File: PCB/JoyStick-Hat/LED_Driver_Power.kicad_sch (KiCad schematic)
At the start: 1 part, among them U2 STP16CPC26XTR

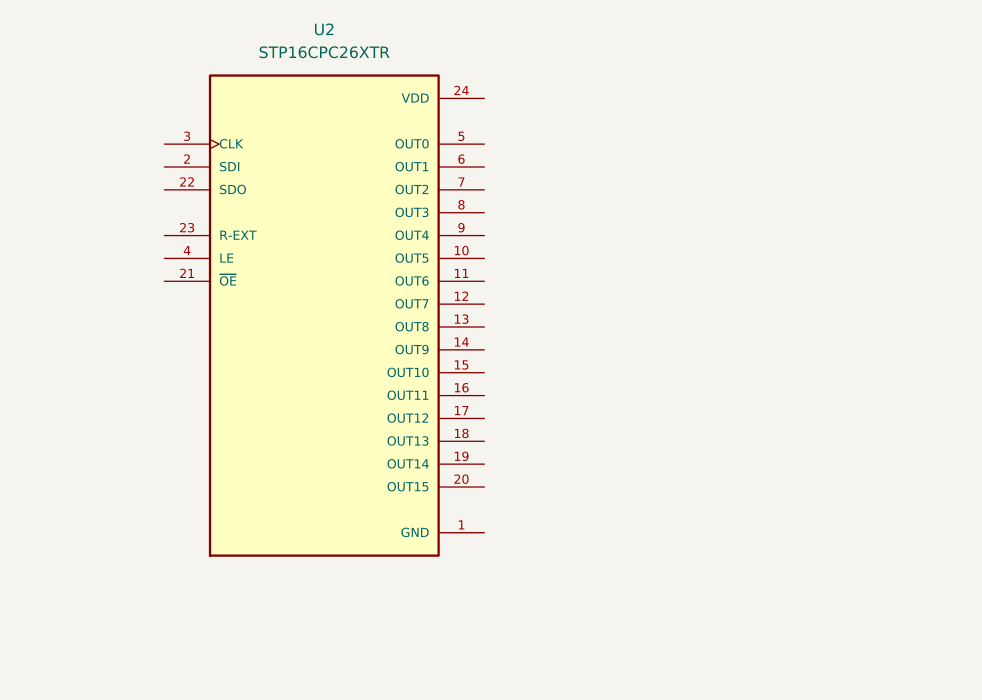
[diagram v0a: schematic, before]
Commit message: Power and LED Driver
Power Supply Schematic sketched out using Pololu power regulator modules to hasten design. LED drivers replaced with ones that have 24 ouputs so we can use 20 unit bar graph LEDs and have 8 extra channels for other onboard LEDs
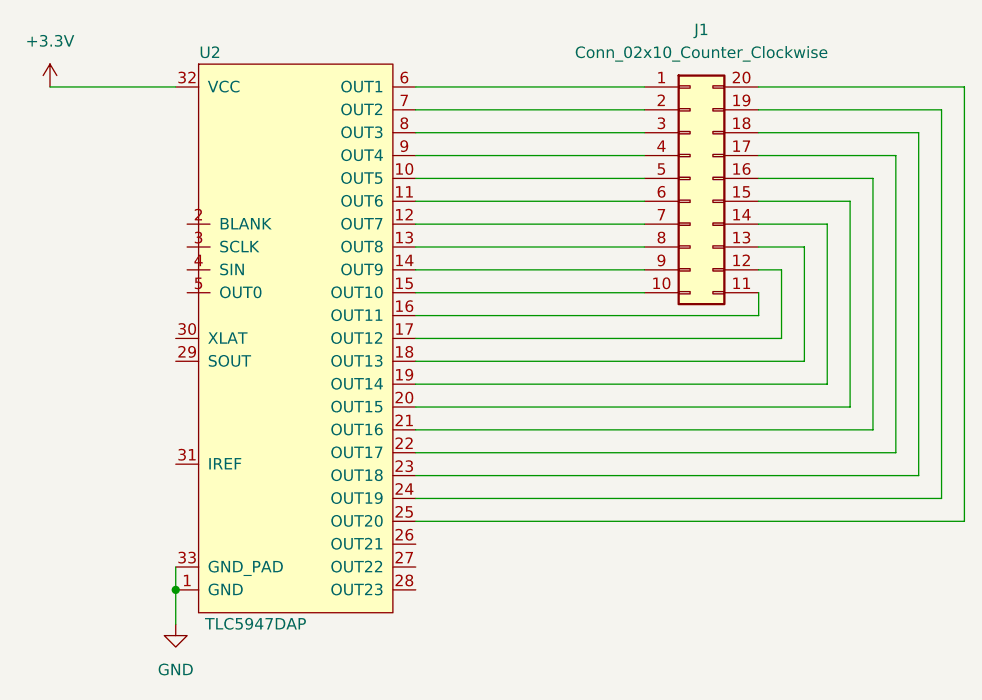
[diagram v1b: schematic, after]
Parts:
- removed U2: STP16CPC26XTR, AVR-KiCAD-Lib-ICs:SOP63P600X173-24N_STP16CPC26XTR, symbol AVR-KiCAD-Lib-ICs:STP16CPC26XTR
- added J1: Conn_02x10_Counter_Clockwise, Connector_PinHeader_2.54mm:PinHeader_2x10_P2.54mm_Vertical, symbol Connector_Generic:Conn_02x10_Counter_Clockwise
- added U2: TLC5947DAP, AVR-KiCAD-Lib-ICs:DAP32_4P36X4P11, symbol AVR-KiCAD-Lib-ICs:TLC5947DAP
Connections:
- new net: J1.1 (Pin_1), U2.6 (OUT1)
- new net: J1.10 (Pin_10), U2.15 (OUT10)
- new net: J1.11 (Pin_11), U2.16 (OUT11)
- new net: J1.12 (Pin_12), U2.17 (OUT12)
- new net: J1.13 (Pin_13), U2.18 (OUT13)
- new net: J1.14 (Pin_14), U2.19 (OUT14)
- new net: J1.15 (Pin_15), U2.20 (OUT15)
- new net: J1.16 (Pin_16), U2.21 (OUT16)
- new net: J1.17 (Pin_17), U2.22 (OUT17)
- new net: J1.18 (Pin_18), U2.23 (OUT18)
- new net: J1.19 (Pin_19), U2.24 (OUT19)
- new net: J1.2 (Pin_2), U2.7 (OUT2)
- new net: J1.20 (Pin_20), U2.25 (OUT20)
- new net: J1.3 (Pin_3), U2.8 (OUT3)
- new net: J1.4 (Pin_4), U2.9 (OUT4)
- new net: J1.5 (Pin_5), U2.10 (OUT5)
- new net: J1.6 (Pin_6), U2.11 (OUT6)
- new net: J1.7 (Pin_7), U2.12 (OUT7)
- new net: J1.8 (Pin_8), U2.13 (OUT8)
- new net: J1.9 (Pin_9), U2.14 (OUT9)
- new net +3.3V: U2.32 (VCC)
- new net GND: U2.1 (GND), U2.33 (GND_PAD)

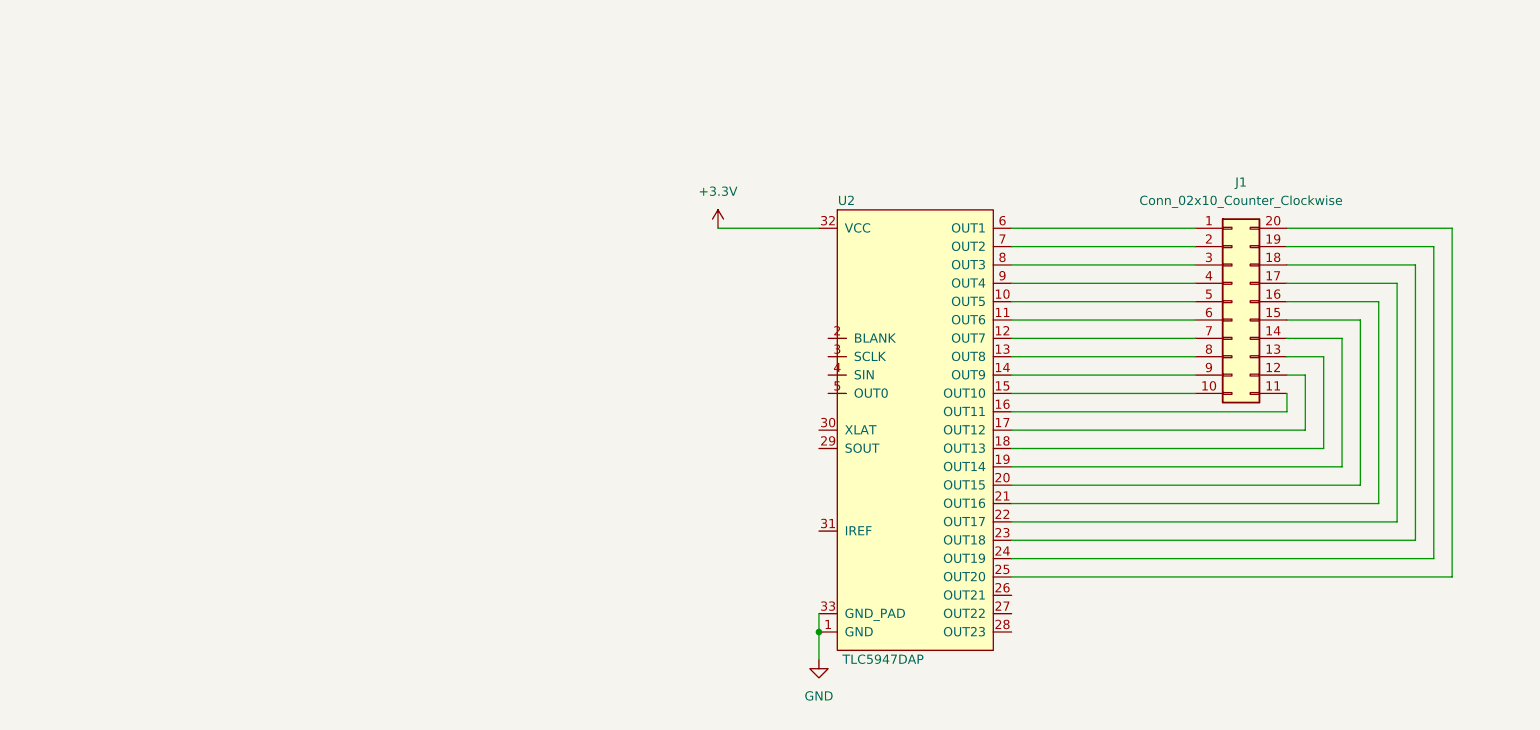
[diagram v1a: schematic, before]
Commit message: LED drivers and Joystick
Finished LED driver scheamtics, corrected some problems with symbols. added conenctors for joystick and buttons, connected RPI pins to MCU
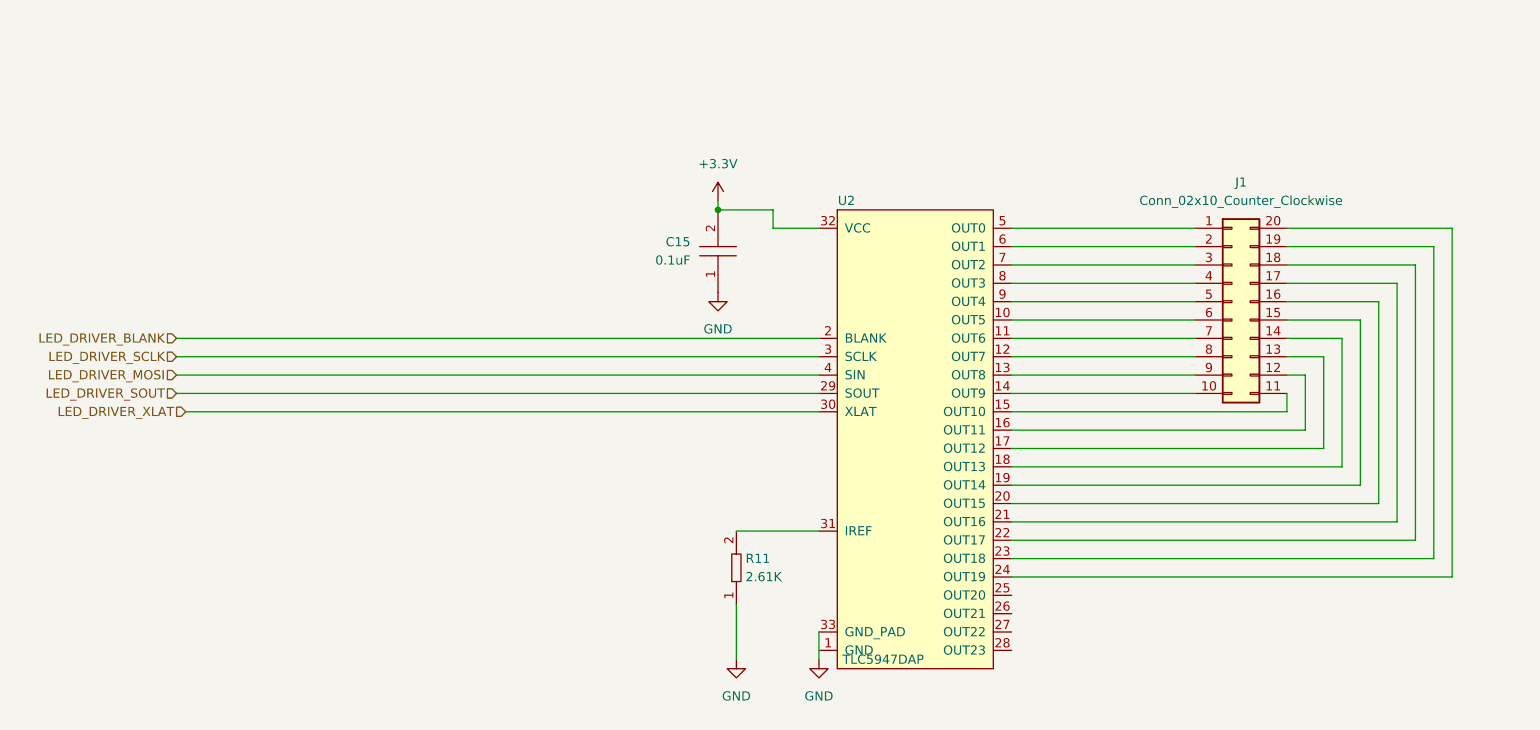
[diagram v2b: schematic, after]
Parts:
- added C15: CL10B104JB8NNNC, AVR-KiCAD-Lib-Capacitors:C0603, symbol AVR-KiCAD-Lib-Capacitors:CL10B104JB8NNNC
- added R11: RMCF0603FT2K61, AVR-KiCAD-Lib-Resistors:R0603, symbol AVR-KiCAD-Lib-Resistors:RMCF0603FT2K61
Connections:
- net +3.3V: now also C15.2
- net GND: now also C15.1, R11.1; no longer U2.1 (GND)
- net at J1.1 (Pin_1): now also U2.5 (OUT0); no longer U2.6 (OUT1)
- net at J1.10 (Pin_10): now also U2.14 (OUT9); no longer U2.15 (OUT10)
- net at J1.11 (Pin_11): now also U2.15 (OUT10); no longer U2.16 (OUT11)
- net at J1.12 (Pin_12): now also U2.16 (OUT11); no longer U2.17 (OUT12)
- net at J1.13 (Pin_13): now also U2.17 (OUT12); no longer U2.18 (OUT13)
- net at J1.14 (Pin_14): now also U2.18 (OUT13); no longer U2.19 (OUT14)
- net at J1.15 (Pin_15): now also U2.19 (OUT14); no longer U2.20 (OUT15)
- net at J1.16 (Pin_16): now also U2.20 (OUT15); no longer U2.21 (OUT16)
- net at J1.17 (Pin_17): now also U2.21 (OUT16); no longer U2.22 (OUT17)
- net at J1.18 (Pin_18): now also U2.22 (OUT17); no longer U2.23 (OUT18)
- net at J1.19 (Pin_19): now also U2.23 (OUT18); no longer U2.24 (OUT19)
- net at J1.2 (Pin_2): now also U2.6 (OUT1); no longer U2.7 (OUT2)
- net at J1.20 (Pin_20): now also U2.24 (OUT19); no longer U2.25 (OUT20)
- net at J1.3 (Pin_3): now also U2.7 (OUT2); no longer U2.8 (OUT3)
- net at J1.4 (Pin_4): now also U2.8 (OUT3); no longer U2.9 (OUT4)
- net at J1.5 (Pin_5): now also U2.9 (OUT4); no longer U2.10 (OUT5)
- net at J1.6 (Pin_6): now also U2.10 (OUT5); no longer U2.11 (OUT6)
- net at J1.7 (Pin_7): now also U2.11 (OUT6); no longer U2.12 (OUT7)
- net at J1.8 (Pin_8): now also U2.12 (OUT7); no longer U2.13 (OUT8)
- net at J1.9 (Pin_9): now also U2.13 (OUT8); no longer U2.14 (OUT9)
- net LED_DRIVER_BLANK: now reaches U2.2 (BLANK)
- net LED_DRIVER_SOUT: now reaches U2.29 (SOUT)
- net LED_DRIVER_SCLK: now reaches U2.3 (SCLK)
- net LED_DRIVER_XLAT: now reaches U2.30 (XLAT)
- net at U2.31 (IREF): now also R11.2
- net LED_DRIVER_MOSI: now reaches U2.4 (SIN)
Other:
- moved on the sheet: U2

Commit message: Schematic Progress
Made progress with schematic and corrected designator letters with connectors to match the built in paradigm of using J instead of T. T will not be used to referencing transformers instead of connectors.
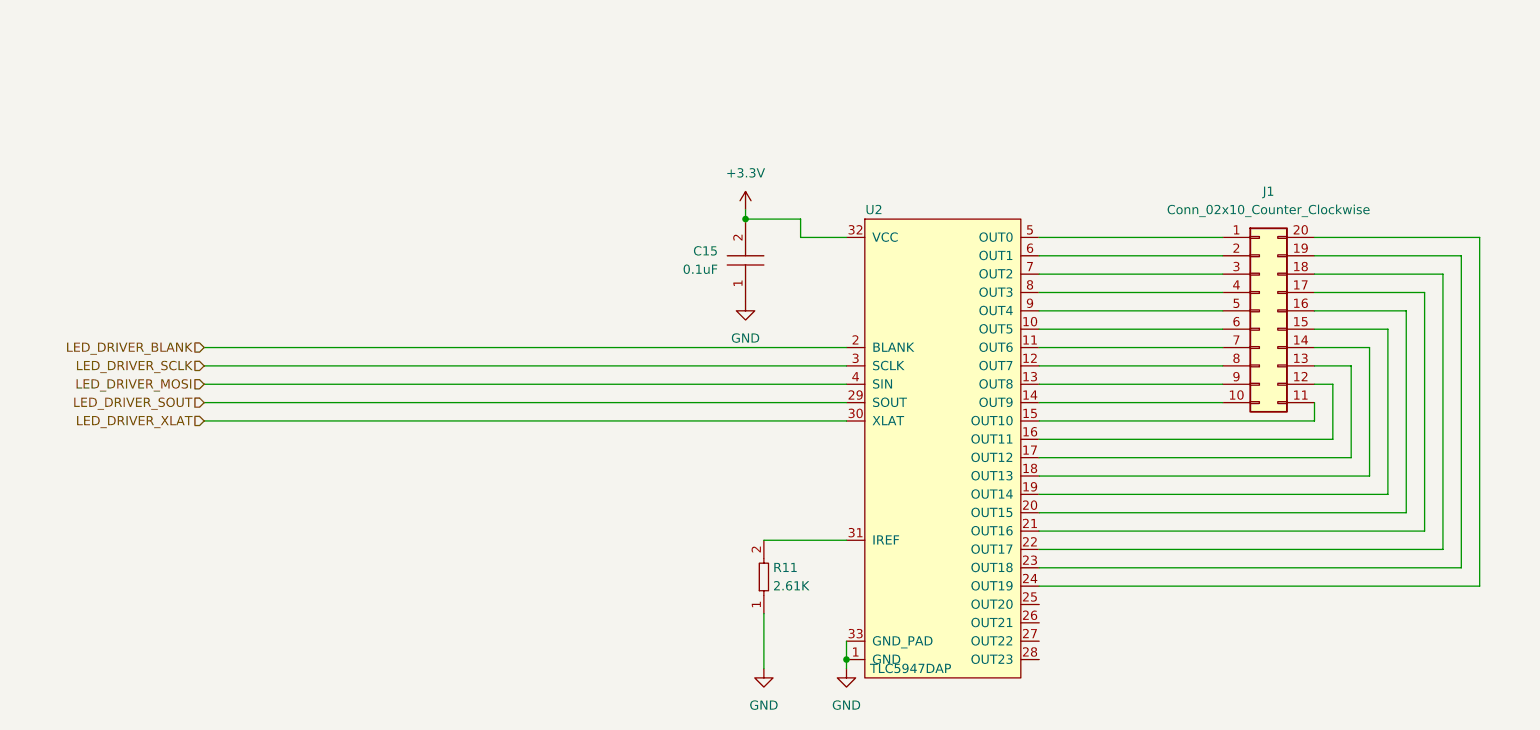
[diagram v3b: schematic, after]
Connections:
- net GND: now also U2.1 (GND)
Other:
- moved on the sheet: C15, J1, R11, U2

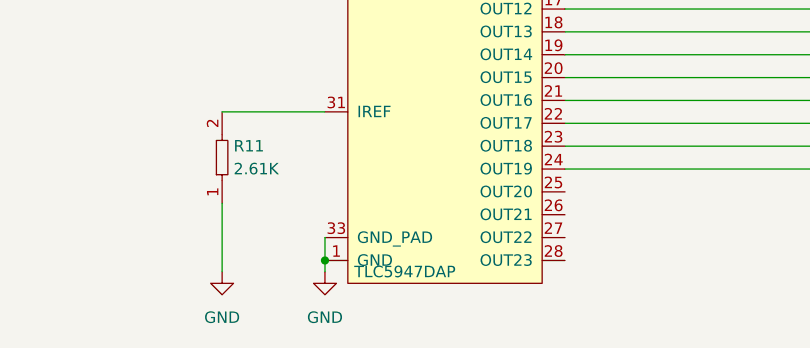
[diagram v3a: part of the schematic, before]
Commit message: Schematic Complete
Schematic completed. Moved to 100 pin version of STM32 MCU for more connectivity and better muxing of internal peripherals with pins.
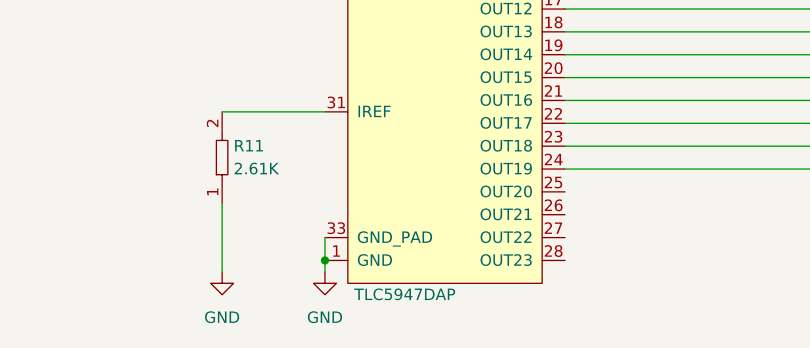
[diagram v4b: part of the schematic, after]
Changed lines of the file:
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@@
       (effects (font (size 1.27 1.27)) hide)
     )
-    (property "_Value_" "TLC5947DAP" (at 133.35 113.03 0)
+    (property "_Value_" "TLC5947DAP" (at 133.35 115.57 0)
       (effects (font (size 1.27 1.27)))
     )

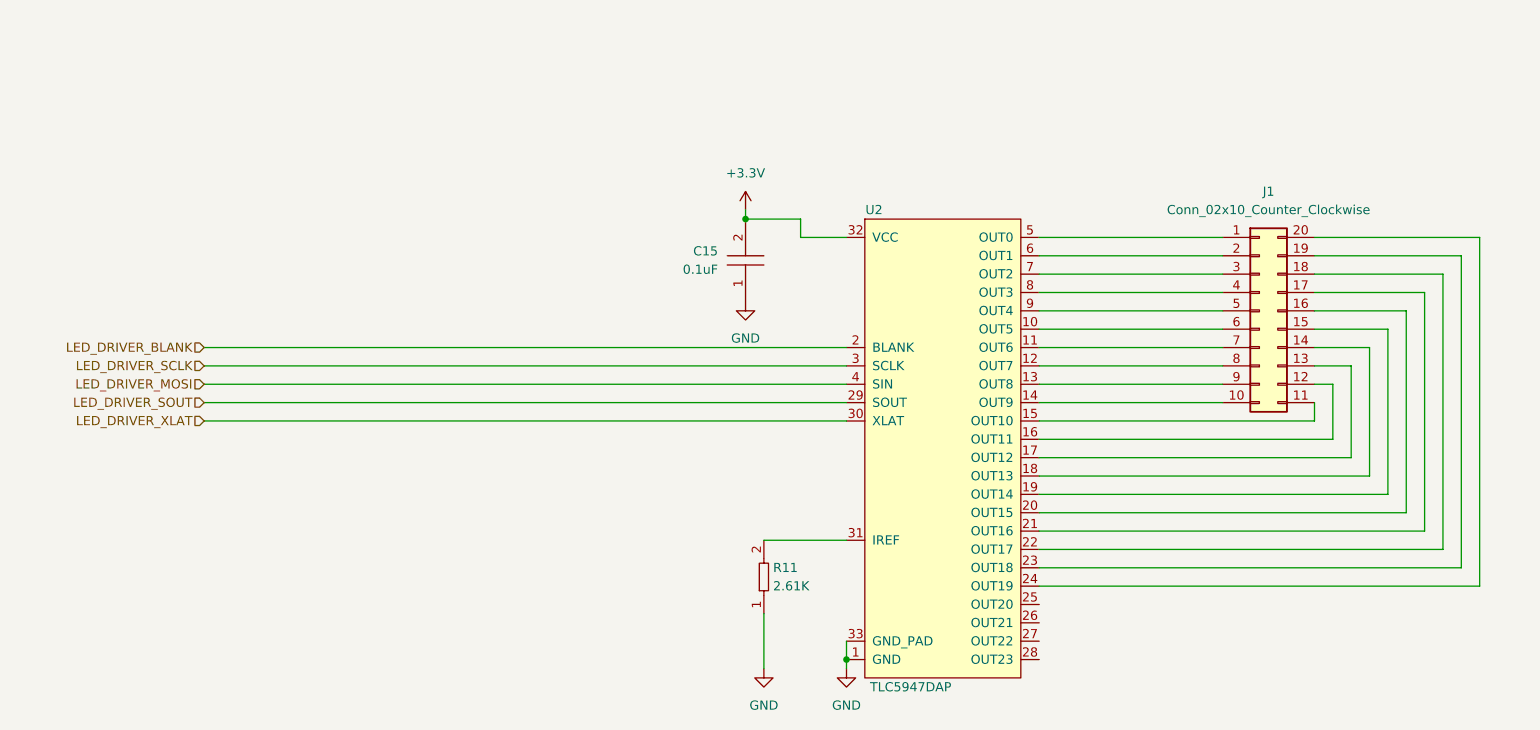
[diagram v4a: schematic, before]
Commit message: LEDs and Additional connectors
Added heartbeat and diagnostic LEDs to STM32 and RPi3 schematics so we can directly flash them for debug purposes. Added a connector for serial port diagnostics on STM32. Added rotary switch interface for STM32 and added pullups to button connectors.
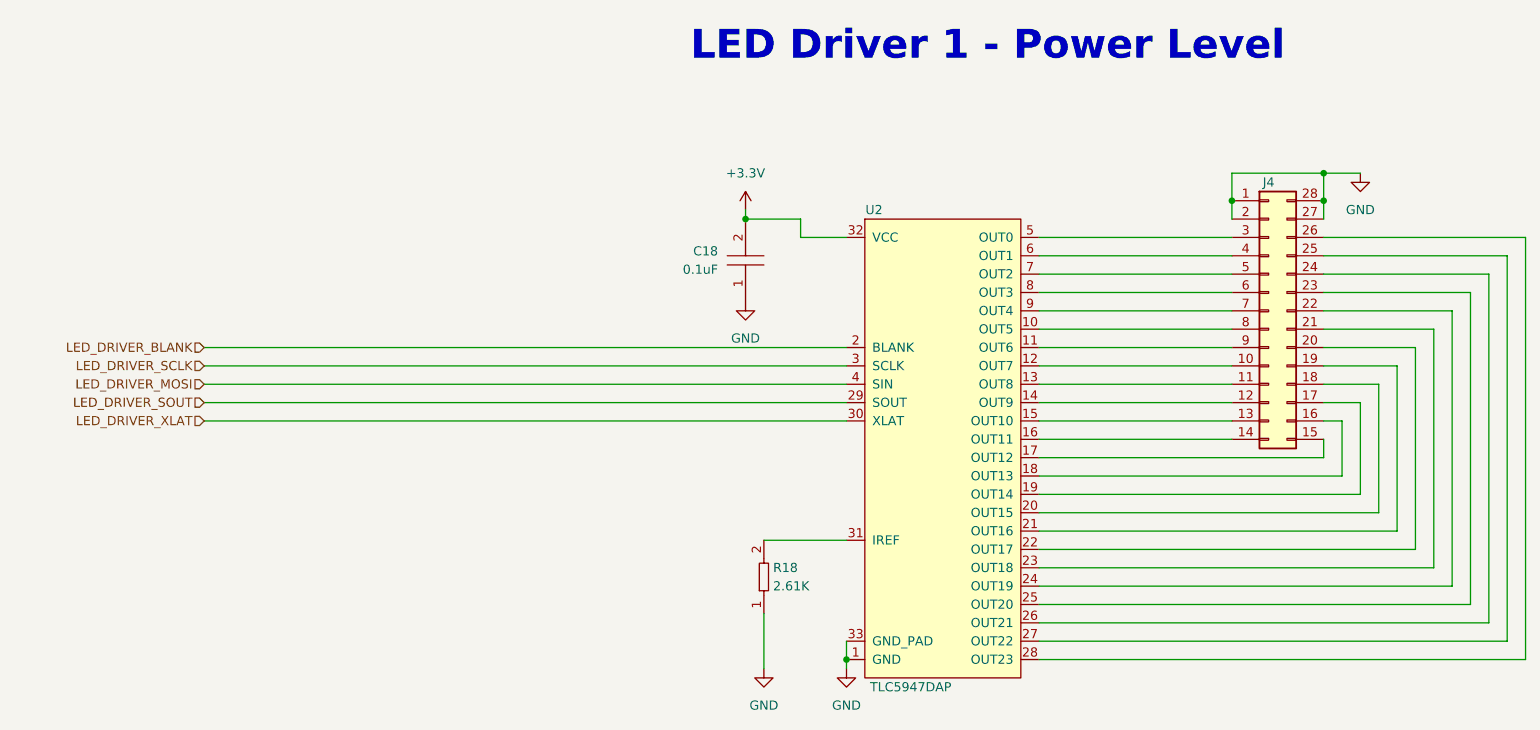
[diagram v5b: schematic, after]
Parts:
- removed J1: Conn_02x10_Counter_Clockwise, Connector_PinHeader_2.54mm:PinHeader_2x10_P2.54mm_Vertical, symbol Connector_Generic:Conn_02x10_Counter_Clockwise
- added J4: Conn_02x14_Counter_Clockwise, Connector_PinHeader_2.54mm:PinHeader_2x14_P2.54mm_Vertical, symbol Connector_Generic:Conn_02x14_Counter_Clockwise
- renumbered C15 to C18, R11 to R18
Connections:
- net GND: now also J4.1 (Pin_1), J4.2 (Pin_2), J4.27 (Pin_27), J4.28 (Pin_28)
- net at U2.5 (OUT0): now also J4.3 (Pin_3)
- net at U2.14 (OUT9): now also J4.12 (Pin_12)
- net at U2.15 (OUT10): now also J4.13 (Pin_13)
- net at U2.16 (OUT11): now also J4.14 (Pin_14)
- net at U2.17 (OUT12): now also J4.15 (Pin_15)
- net at U2.18 (OUT13): now also J4.16 (Pin_16)
- net at U2.19 (OUT14): now also J4.17 (Pin_17)
- net at U2.20 (OUT15): now also J4.18 (Pin_18)
- net at U2.21 (OUT16): now also J4.19 (Pin_19)
- net at U2.22 (OUT17): now also J4.20 (Pin_20)
- net at U2.23 (OUT18): now also J4.21 (Pin_21)
- net at U2.6 (OUT1): now also J4.4 (Pin_4)
- net at U2.24 (OUT19): now also J4.22 (Pin_22)
- net at U2.7 (OUT2): now also J4.5 (Pin_5)
- net at U2.8 (OUT3): now also J4.6 (Pin_6)
- net at U2.9 (OUT4): now also J4.7 (Pin_7)
- net at U2.10 (OUT5): now also J4.8 (Pin_8)
- net at U2.11 (OUT6): now also J4.9 (Pin_9)
- net at U2.12 (OUT7): now also J4.10 (Pin_10)
- net at U2.13 (OUT8): now also J4.11 (Pin_11)
- net at U2.25 (OUT20): now also J4.23 (Pin_23)
- net at U2.26 (OUT21): now also J4.24 (Pin_24)
- net at U2.27 (OUT22): now also J4.25 (Pin_25)
- net at U2.28 (OUT23): now also J4.26 (Pin_26)
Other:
- note added: "LED Driver 1 - Power Level"
